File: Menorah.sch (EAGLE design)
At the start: 34 parts

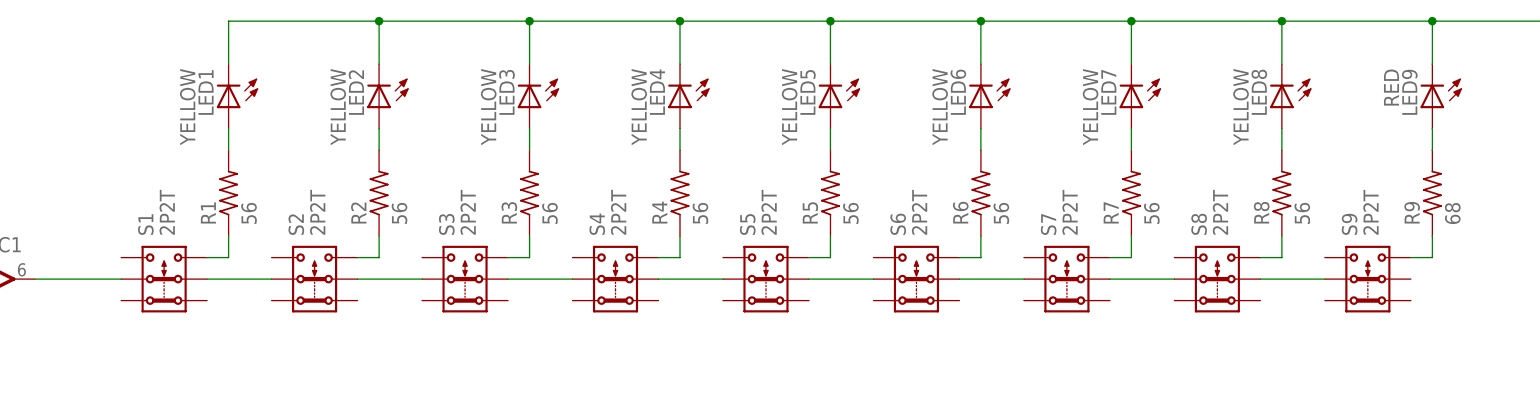
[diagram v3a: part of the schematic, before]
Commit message: replaced dpdt switch
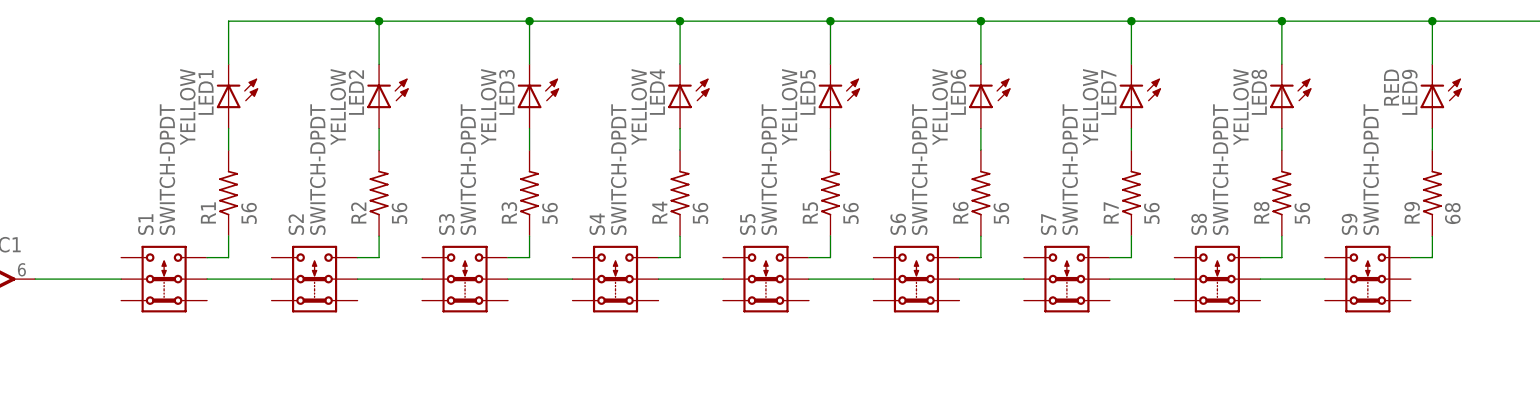
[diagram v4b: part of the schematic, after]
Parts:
- S1, S2, S3, S4, S5, S6, S7, S8, S9: value 2P2T -> SWITCH-DPDT; device switch:2P2T -> Menorah:SWITCH-DPDT
- S10: DIGIKEY (none) -> EG4791-ND
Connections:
- net N$10: now also S1.3; no longer S1.3.2
- net N$11: now also S2.3; no longer S2.3.2
- net N$12: now also S3.3; no longer S3.3.2
- net N$13: now also S4.3; no longer S4.3.2
- net N$14: now also S5.3; no longer S5.3.2
- net N$15: now also S6.3; no longer S6.3.2
- net N$16: now also S7.3; no longer S7.3.2
- net N$17: now also S8.3; no longer S8.3.2
- net N$18: now also S9.3; no longer S9.3.2
- net N$21: now also S1.5; no longer S1.2.1
- net N$23: now also S1.2, S2.5; no longer S1.2.2, S2.2.1
- net N$24: now also S2.2, S3.5; no longer S2.2.2, S3.2.1
- net N$25: now also S3.2, S4.5; no longer S3.2.2, S4.2.1
- net N$26: now also S4.2, S5.5; no longer S4.2.2, S5.2.1
- net N$27: now also S5.2, S6.5; no longer S5.2.2, S6.2.1
- net N$28: now also S6.2, S7.5; no longer S6.2.2, S7.2.1
- net N$29: now also S7.2, S8.5; no longer S7.2.2, S8.2.1
- net N$30: now also S8.2, S9.5; no longer S8.2.2, S9.2.1
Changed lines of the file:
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@@
 </classes>
 <parts>
-<part name="S1" library="switch" deviceset="2P2T" device="">
+<part name="S1" library="Menorah" deviceset="SWITCH-DPDT" device="">
 <attribute name="DIGIKEY" value="401-2002-1-ND"/>
 </part>
@@
 <attribute name="DIGIKEY" value="1276-5502-1-ND"/>
 </part>
-<part name="S2" library="switch" deviceset="2P2T" device="">
-<attribute name="DIGIKEY" value="401-2002-1-ND"/>
-</part>
-<part name="S3" library="switch" deviceset="2P2T" device="">
-<attribute name="DIGIKEY" value="401-2002-1-ND"/>
-</part>
-<part name="S4" library="switch" deviceset="2P2T" device="">
-<attribute name="DIGIKEY" value="401-2002-1-ND"/>
-</part>
-<part name="S5" library="switch" deviceset="2P2T" device="">
-<attribute name="DIGIKEY" value="401-2002-1-ND"/>
-</part>
-<part name="S6" library="switch" deviceset="2P2T" device="">
-<attribute name="DIGIKEY" value="401-2002-1-ND"/>
-</part>
-<part name="S7" library="switch" deviceset="2P2T" device="">
-<attribute name="DIGIKEY" value="401-2002-1-ND"/>
-</part>
-<part name="S8" library="switch" deviceset="2P2T" device="">
-<attribute name="DIGIKEY" value="401-2002-1-ND"/>
-</part>
-<part name="S9" library="switch" deviceset="2P2T" device="">
-<attribute name="DIGIKEY" value="401-2002-1-ND"/>
-</part>
-<part name="S10" library="Menorah" deviceset="SWITCH-SPST" device=""/>
+<part name="S2" library="Menorah" deviceset="SWITCH-DPDT" device="">
+<attribute name="DIGIKEY" value="401-2002-1-ND"/>
+</part>
+<part name="S3" library="Menorah" deviceset="SWITCH-DPDT" device="">
+<attribute name="DIGIKEY" value="401-2002-1-ND"/>
+</part>
+<part name="S4" library="Menorah" deviceset="SWITCH-DPDT" device="">
+<attribute name="DIGIKEY" value="401-2002-1-ND"/>
+</part>
+<part name="S5" library="Menorah" deviceset="SWITCH-DPDT" device="">
+<attribute name="DIGIKEY" value="401-2002-1-ND"/>
+</part>
+<part name="S6" library="Menorah" deviceset="SWITCH-DPDT" device="">
+<attribute name="DIGIKEY" value="401-2002-1-ND"/>
+</part>
+<part name="S7" library="Menorah" deviceset="SWITCH-DPDT" device="">
+<attribute name="DIGIKEY" value="401-2002-1-ND"/>
+</part>
+<part name="S8" library="Menorah" deviceset="SWITCH-DPDT" device="">
+<attribute name="DIGIKEY" value="401-2002-1-ND"/>
+</part>
+<part name="S9" library="Menorah" deviceset="SWITCH-DPDT" device="">
+<attribute name="DIGIKEY" value="401-2002-1-ND"/>
+</part>
+<part name="S10" library="Menorah" deviceset="SWITCH-SPST" device="">
+<attribute name="DIGIKEY" value="EG4791-ND"/>
+</part>
 </parts>
 <sheets>
@@
 </plain>
 <instances>
-<instance part="S1" gate="G$1" x="162.56" y="132.08" rot="R90">
+<instance part="S1" gate="S$1" x="162.56" y="132.08" rot="R90">
 <attribute name="DIGIKEY" x="162.56" y="132.08" size="1.778" layer="96" rot="R90" display="off"/>
 </instance>
@@
 <attribute name="DIGIKEY" x="294.64" y="142.24" size="1.778" layer="96" rot="R90" display="off"/>
 </instance>
-<instance part="S2" gate="G$1" x="180.34" y="132.08" rot="R90">
+<instance part="S2" gate="S$1" x="180.34" y="132.08" rot="R90">
 <attribute name="DIGIKEY" x="180.34" y="132.08" size="1.778" layer="96" rot="R90" display="off"/>
 </instance>
-<instance part="S3" gate="G$1" x="198.12" y="132.08" rot="R90">
+<instance part="S3" gate="S$1" x="198.12" y="132.08" rot="R90">
 <attribute name="DIGIKEY" x="198.12" y="132.08" size="1.778" layer="96" rot="R90" display="off"/>
 </instance>
-<instance part="S4" gate="G$1" x="215.9" y="132.08" rot="R90">
+<instance part="S4" gate="S$1" x="215.9" y="132.08" rot="R90">
 <attribute name="DIGIKEY" x="215.9" y="132.08" size="1.778" layer="96" rot="R90" display="off"/>
 </instance>
-<instance part="S5" gate="G$1" x="233.68" y="132.08" rot="R90">
+<instance part="S5" gate="S$1" x="233.68" y="132.08" rot="R90">
 <attribute name="DIGIKEY" x="233.68" y="132.08" size="1.778" layer="96" rot="R90" display="off"/>
 </instance>
-<instance part="S6" gate="G$1" x="251.46" y="132.08" rot="R90">
+<instance part="S6" gate="S$1" x="251.46" y="132.08" rot="R90">
 <attribute name="DIGIKEY" x="251.46" y="132.08" size="1.778" layer="96" rot="R90" display="off"/>
 </instance>
-<instance part="S7" gate="G$1" x="269.24" y="132.08" rot="R90">
+<instance part="S7" gate="S$1" x="269.24" y="132.08" rot="R90">
 <attribute name="DIGIKEY" x="269.24" y="132.08" size="1.778" layer="96" rot="R90" display="off"/>
 </instance>
-<instance part="S8" gate="G$1" x="287.02" y="132.08" rot="R90">
+<instance part="S8" gate="S$1" x="287.02" y="132.08" rot="R90">
 <attribute name="DIGIKEY" x="287.02" y="132.08" size="1.778" layer="96" rot="R90" display="off"/>
 </instance>
-<instance part="S9" gate="G$1" x="304.8" y="132.08" rot="R90">
+<instance part="S9" gate="S$1" x="304.8" y="132.08" rot="R90">
 <attribute name="DIGIKEY" x="304.8" y="132.08" size="1.778" layer="96" rot="R90" display="off"/>
 </instance>
-<instance part="S10" gate="G$1" x="63.5" y="134.62"/>
+<instance part="S10" gate="G$1" x="63.5" y="134.62">
+<attribute name="DIGIKEY" x="63.5" y="134.62" size="1.778" layer="96" display="off"/>
+</instance>
 </instances>
 <busses>
@@
 <segment>
 <pinref part="IC1" gate="A" pin="OUT"/>
-<pinref part="S1" gate="G$1" pin="2.1"/>
+<pinref part="S1" gate="S$1" pin="5"/>
 <wire x1="147.32" y1="132.08" x2="157.48" y2="132.08" width="0.1524" layer="91"/>
 </segment>
@@
 <net name="N$23" class="0">
 <segment>
-<pinref part="S1" gate="G$1" pin="2.2"/>
+<pinref part="S1" gate="S$1" pin="2"/>
 <wire x1="167.64" y1="132.08" x2="175.26" y2="132.08" width="0.1524" layer="91"/>
-<pinref part="S2" gate="G$1" pin="2.1"/>
+<pinref part="S2" gate="S$1" pin="5"/>
 </segment>
 </net>
@@
 <segment>
 <wire x1="185.42" y1="132.08" x2="193.04" y2="132.08" width="0.1524" layer="91"/>
-<pinref part="S2" gate="G$1" pin="2.2"/>
-<pinref part="S3" gate="G$1" pin="2.1"/>
+<pinref part="S2" gate="S$1" pin="2"/>
+<pinref part="S3" gate="S$1" pin="5"/>
 </segment>
 </net>
@@
 <segment>
 <wire x1="203.2" y1="132.08" x2="210.82" y2="132.08" width="0.1524" layer="91"/>
-<pinref part="S3" gate="G$1" pin="2.2"/>
-<pinref part="S4" gate="G$1" pin="2.1"/>
+<pinref part="S3" gate="S$1" pin="2"/>
+<pinref part="S4" gate="S$1" pin="5"/>
 </segment>
 </net>
@@
 <segment>
 <wire x1="220.98" y1="132.08" x2="228.6" y2="132.08" width="0.1524" layer="91"/>
-<pinref part="S4" gate="G$1" pin="2.2"/>
-<pinref part="S5" gate="G$1" pin="2.1"/>
+<pinref part="S4" gate="S$1" pin="2"/>
+<pinref part="S5" gate="S$1" pin="5"/>
 </segment>
 </net>
@@
 <segment>
 <wire x1="238.76" y1="132.08" x2="246.38" y2="132.08" width="0.1524" layer="91"/>
-<pinref part="S5" gate="G$1" pin="2.2"/>
-<pinref part="S6" gate="G$1" pin="2.1"/>
+<pinref part="S5" gate="S$1" pin="2"/>
+<pinref part="S6" gate="S$1" pin="5"/>
 </segment>
 </net>
@@
 <segment>
 <wire x1="256.54" y1="132.08" x2="264.16" y2="132.08" width="0.1524" layer="91"/>
-<pinref part="S6" gate="G$1" pin="2.2"/>
-<pinref part="S7" gate="G$1" pin="2.1"/>
+<pinref part="S6" gate="S$1" pin="2"/>
+<pinref part="S7" gate="S$1" pin="5"/>
 </segment>
 </net>
@@
 <segment>
 <wire x1="274.32" y1="132.08" x2="281.94" y2="132.08" width="0.1524" layer="91"/>
-<pinref part="S7" gate="G$1" pin="2.2"/>
-<pinref part="S8" gate="G$1" pin="2.1"/>
+<pinref part="S7" gate="S$1" pin="2"/>
+<pinref part="S8" gate="S$1" pin="5"/>
 </segment>
 </net>
@@
 <segment>
 <wire x1="292.1" y1="132.08" x2="299.72" y2="132.08" width="0.1524" layer="91"/>
-<pinref part="S8" gate="G$1" pin="2.2"/>
-<pinref part="S9" gate="G$1" pin="2.1"/>
+<pinref part="S8" gate="S$1" pin="2"/>
+<pinref part="S9" gate="S$1" pin="5"/>
 </segment>
 </net>
 <net name="N$10" class="0">
 <segment>
-<pinref part="S1" gate="G$1" pin="3.2"/>
+<pinref part="S1" gate="S$1" pin="3"/>
 <wire x1="167.64" y1="134.62" x2="170.18" y2="134.62" width="0.1524" layer="91"/>
 <pinref part="R1" gate="G$1" pin="1"/>
@@
 <wire x1="187.96" y1="134.62" x2="187.96" y2="137.16" width="0.1524" layer="91"/>
 <pinref part="R2" gate="G$1" pin="1"/>
-<pinref part="S2" gate="G$1" pin="3.2"/>
+<pinref part="S2" gate="S$1" pin="3"/>
 </segment>
 </net>
@@
 <wire x1="205.74" y1="134.62" x2="205.74" y2="137.16" width="0.1524" layer="91"/>
 <pinref part="R3" gate="G$1" pin="1"/>
-<pinref part="S3" gate="G$1" pin="3.2"/>
+<pinref part="S3" gate="S$1" pin="3"/>
 </segment>
 </net>
@@
 <wire x1="223.52" y1="134.62" x2="223.52" y2="137.16" width="0.1524" layer="91"/>
 <pinref part="R4" gate="G$1" pin="1"/>
-<pinref part="S4" gate="G$1" pin="3.2"/>
+<pinref part="S4" gate="S$1" pin="3"/>
 </segment>
 </net>
@@
 <wire x1="241.3" y1="134.62" x2="241.3" y2="137.16" width="0.1524" layer="91"/>
 <pinref part="R5" gate="G$1" pin="1"/>
-<pinref part="S5" gate="G$1" pin="3.2"/>
+<pinref part="S5" gate="S$1" pin="3"/>
 </segment>
 </net>
@@
 <wire x1="259.08" y1="134.62" x2="259.08" y2="137.16" width="0.1524" layer="91"/>
 <pinref part="R6" gate="G$1" pin="1"/>
-<pinref part="S6" gate="G$1" pin="3.2"/>
+<pinref part="S6" gate="S$1" pin="3"/>
 </segment>
 </net>
@@
 <wire x1="276.86" y1="134.62" x2="276.86" y2="137.16" width="0.1524" layer="91"/>
 <pinref part="R7" gate="G$1" pin="1"/>
-<pinref part="S7" gate="G$1" pin="3.2"/>
+<pinref part="S7" gate="S$1" pin="3"/>
 </segment>
 </net>
@@
 <wire x1="294.64" y1="134.62" x2="294.64" y2="137.16" width="0.1524" layer="91"/>
 <pinref part="R8" gate="G$1" pin="1"/>
-<pinref part="S8" gate="G$1" pin="3.2"/>
+<pinref part="S8" gate="S$1" pin="3"/>
 </segment>
 </net>
@@
 <pinref part="R9" gate="G$1" pin="1"/>
 <wire x1="312.42" y1="134.62" x2="312.42" y2="137.16" width="0.1524" layer="91"/>
-<pinref part="S9" gate="G$1" pin="3.2"/>
-</segment>
-</net>
+<pinref part="S9" gate="S$1" pin="3"/>
+</segment>
+</net>

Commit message: changed circircuit, updated pcb
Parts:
- removed G1: CR2032, Menorah:CR2032
- removed IC1: (no value), linear:1AMP_P7+4D
- removed R12: 100k, rcl:R-US_R0805
- added Q1: BUZ382, transistor-fet:BUZ382
- R1, R2, R3, R4, R5, R6, R7, R8: value 56 -> 100; DIGIKEY 1276-5502-1-ND -> 1276-5508-1-ND
- R11: value 51k -> 100; DIGIKEY 1276-5569-1-ND -> 1276-5508-1-ND
- R9: value 68 -> 100; DIGIKEY 1276-5504-1-ND -> 1276-5508-1-ND
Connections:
- removed net N$23: S1.2, S2.5
- removed net N$24: S2.2, S3.5
- removed net N$25: S3.2, S4.5
- removed net N$26: S4.2, S5.5
- removed net N$27: S5.2, S6.5
- removed net N$28: S6.2, S7.5
- removed net N$29: S7.2, S8.5
- removed net N$30: S8.2, S9.5
- net N$1: now also LED1.C, R1.1; no longer LED1.A, R1.2
- net N$10: now also R1.2; no longer R1.1
- net N$11: now also R2.2; no longer R2.1
- net N$12: now also R3.2; no longer R3.1
- net N$13: now also R4.2; no longer R4.1
- net N$14: now also R5.2; no longer R5.1
- net N$15: now also R6.2; no longer R6.1
- net N$16: now also R7.2; no longer R7.1
- net N$17: now also R8.2; no longer R8.1
- net N$18: now also R9.2; no longer R9.1
- net N$19: now also R11.2, S10.1@A, S10.1@B; no longer IC1.-IN, R11.1, R12.2
- net N$2: now also LED2.C, R2.1; no longer LED2.A, R2.2
- net N$21: now also Q1.D, S1.2, S2.2, S2.5, S3.2, S3.5, S4.2, S4.5, S5.2, S5.5, S6.2, S6.5, S7.2, S7.5, S8.2, S8.5, S9.2, S9.5; no longer IC1.OUT
- net N$22: now also Q1.G, R11.1; no longer IC1.+IN, S10.1@A, S10.1@B
- net N$3: now also LED3.C, R3.1; no longer LED3.A, R3.2
- net N$4: now also LED4.C, R4.1; no longer LED4.A, R4.2
- net N$5: now also LED5.C, R5.1; no longer LED5.A, R5.2
- net N$6: now also LED6.C, R6.1; no longer LED6.A, R6.2
- net N$7: now also LED7.C, R7.1; no longer LED7.A, R7.2
- net N$8: now also LED8.C, R8.1; no longer LED8.A, R8.2
- net N$9: now also LED9.C, R9.1; no longer LED9.A, R9.2
- net PE: now also LED1.A, LED2.A, LED3.A, LED4.A, LED5.A, LED6.A, LED7.A, LED8.A, LED9.A, Q1.S; no longer G1.-, IC1.V-, LED1.C, LED2.C, LED3.C, LED4.C, LED5.C, LED6.C, LED7.C, LED8.C, LED9.C, R11.2
- net VCC: no longer G1.+, IC1.V+, R12.1
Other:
- moved on the sheet: C1, LED1, LED2, LED3, LED4, LED5, LED6, LED7, LED8, LED9, R1, R10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

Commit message: design finished
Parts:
- Q1: value BUZ382 -> (none); device transistor-fet:BUZ382 -> transistors:2N7002A_SOT23
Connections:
- net PE: no longer LED1.A, LED2.A, LED3.A, LED4.A, LED5.A, LED6.A, LED7.A, LED8.A, LED9.A
- net VCC: now also LED1.A, LED2.A, LED3.A, LED4.A, LED5.A, LED6.A, LED7.A, LED8.A, LED9.A
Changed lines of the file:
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@@
 <attribute name="DIGIKEY" value="475-1415-1-ND"/>
 </part>
-<part name="GND" library="supply1" deviceset="PE" device=""/>
 <part name="C1" library="rcl" deviceset="C-US" device="C1206" value="100uF">
 <attribute name="DIGIKEY" value="490-4539-1-ND"/>
@@
 <attribute name="DIGIKEY" value="EG4791-ND"/>
 </part>
-<part name="Q1" library="transistor-fet" deviceset="BUZ382" device=""/>
 <part name="GND1" library="supply1" deviceset="PE" device=""/>
 <part name="R11" library="rcl" deviceset="R-US_" device="R0805" value="100">
@@
 <attribute name="DIGIKEY" value="1276-5508-1-ND"/>
 </part>
+<part name="P+2" library="supply1" deviceset="VCC" device=""/>
+<part name="Q1" library="transistors" deviceset="2N700*" device="_SOT23" technology="2A"/>
 </parts>
 <sheets>
@@
 <attribute name="DIGIKEY" x="312.42" y="154.94" size="1.778" layer="96" display="off"/>
 </instance>
-<instance part="GND" gate="M" x="327.66" y="152.4" smashed="yes"/>
 <instance part="C1" gate="G$1" x="83.82" y="119.38">
 <attribute name="DIGIKEY" x="83.82" y="119.38" size="1.778" layer="96" display="off"/>
@@
 <attribute name="DIGIKEY" x="63.5" y="127" size="1.778" layer="96" display="off"/>
 </instance>
-<instance part="Q1" gate="G$1" x="121.92" y="129.54"/>
-<instance part="GND1" gate="M" x="127" y="114.3" smashed="yes"/>
+<instance part="GND1" gate="M" x="116.84" y="114.3" smashed="yes"/>
 <instance part="R11" gate="G$1" x="76.2" y="127" rot="R180">
 <attribute name="DIGIKEY" x="76.2" y="127" size="1.778" layer="96" rot="R180" display="off"/>
@@
 <attribute name="DIGIKEY" x="312.42" y="142.24" size="1.778" layer="96" rot="R270" display="off"/>
 </instance>
+<instance part="P+2" gate="VCC" x="170.18" y="177.8"/>
+<instance part="Q1" gate="G$1" x="116.84" y="129.54"/>
 </instances>
 <busses>
@@
 <net name="PE" class="0">
 <segment>
+<pinref part="C1" gate="G$1" pin="2"/>
+<pinref part="GND2" gate="M" pin="PE"/>
+<wire x1="83.82" y1="114.3" x2="83.82" y2="109.22" width="0.1524" layer="91"/>
+</segment>
+<segment>
+<pinref part="GND5" gate="M" pin="PE"/>
+<pinref part="R10" gate="G$1" pin="1"/>
+<wire x1="96.52" y1="109.22" x2="96.52" y2="111.76" width="0.1524" layer="91"/>
+</segment>
+<segment>
+<pinref part="GND1" gate="M" pin="PE"/>
+<wire x1="116.84" y1="116.84" x2="116.84" y2="119.38" width="0.1524" layer="91"/>
+<pinref part="Q1" gate="G$1" pin="S"/>
+</segment>
+</net>
+<net name="VCC" class="0">
+<segment>
+<pinref part="P+1" gate="VCC" pin="VCC"/>
+<wire x1="48.26" y1="137.16" x2="48.26" y2="127" width="0.1524" layer="91"/>
+<pinref part="S10" gate="G$1" pin="0@A"/>
+<wire x1="55.88" y1="127" x2="48.26" y2="127" width="0.1524" layer="91"/>
+<pinref part="S10" gate="G$1" pin="0@B"/>
+<wire x1="55.88" y1="124.46" x2="55.88" y2="127" width="0.1524" layer="91"/>
+<junction x="55.88" y="127"/>
+</segment>
+<segment>
+<pinref part="P+2" gate="VCC" pin="VCC"/>
+<wire x1="170.18" y1="175.26" x2="170.18" y2="162.56" width="0.1524" layer="91"/>
 <wire x1="170.18" y1="162.56" x2="187.96" y2="162.56" width="0.1524" layer="91"/>
 <wire x1="187.96" y1="162.56" x2="205.74" y2="162.56" width="0.1524" layer="91"/>
@@
 <wire x1="276.86" y1="162.56" x2="294.64" y2="162.56" width="0.1524" layer="91"/>
 <wire x1="294.64" y1="162.56" x2="312.42" y2="162.56" width="0.1524" layer="91"/>
-<wire x1="312.42" y1="162.56" x2="327.66" y2="162.56" width="0.1524" layer="91"/>
-<wire x1="327.66" y1="162.56" x2="327.66" y2="154.94" width="0.1524" layer="91"/>
-<pinref part="GND" gate="M" pin="PE"/>
 <pinref part="LED1" gate="G$1" pin="A"/>
 <wire x1="170.18" y1="157.48" x2="170.18" y2="162.56" width="0.1524" layer="91"/>
@@
 <pinref part="LED9" gate="G$1" pin="A"/>
 <wire x1="312.42" y1="157.48" x2="312.42" y2="162.56" width="0.1524" layer="91"/>
-<junction x="312.42" y="162.56"/>
 <pinref part="LED8" gate="G$1" pin="A"/>
 <wire x1="294.64" y1="157.48" x2="294.64" y2="162.56" width="0.1524" layer="91"/>
 <junction x="294.64" y="162.56"/>
-</segment>
-<segment>
-<pinref part="C1" gate="G$1" pin="2"/>
-<pinref part="GND2" gate="M" pin="PE"/>
-<wire x1="83.82" y1="114.3" x2="83.82" y2="109.22" width="0.1524" layer="91"/>
-</segment>
-<segment>
-<pinref part="GND5" gate="M" pin="PE"/>
-<pinref part="R10" gate="G$1" pin="1"/>
-<wire x1="96.52" y1="109.22" x2="96.52" y2="111.76" width="0.1524" layer="91"/>
-</segment>
-<segment>
-<pinref part="GND1" gate="M" pin="PE"/>
-<pinref part="Q1" gate="G$1" pin="S"/>
-<wire x1="127" y1="116.84" x2="127" y2="127" width="0.1524" layer="91"/>
-</segment>
-</net>
-<net name="VCC" class="0">
-<segment>
-<pinref part="P+1" gate="VCC" pin="VCC"/>
-<wire x1="48.26" y1="137.16" x2="48.26" y2="127" width="0.1524" layer="91"/>
-<pinref part="S10" gate="G$1" pin="0@A"/>
-<wire x1="55.88" y1="127" x2="48.26" y2="127" width="0.1524" layer="91"/>
-<pinref part="S10" gate="G$1" pin="0@B"/>
-<wire x1="55.88" y1="124.46" x2="55.88" y2="127" width="0.1524" layer="91"/>
-<junction x="55.88" y="127"/>
+<junction x="170.18" y="162.56"/>
 </segment>
 </net>
@@
 <wire x1="312.42" y1="132.08" x2="309.88" y2="132.08" width="0.1524" layer="91"/>
 <pinref part="Q1" gate="G$1" pin="D"/>
-<wire x1="152.4" y1="132.08" x2="127" y2="132.08" width="0.1524" layer="91"/>
+<wire x1="116.84" y1="139.7" x2="152.4" y2="139.7" width="0.1524" layer="91"/>
+<wire x1="152.4" y1="139.7" x2="152.4" y2="132.08" width="0.1524" layer="91"/>
 </segment>
 </net>
@@
 <wire x1="96.52" y1="127" x2="83.82" y2="127" width="0.1524" layer="91"/>
 <wire x1="96.52" y1="121.92" x2="96.52" y2="127" width="0.1524" layer="91"/>
-<pinref part="Q1" gate="G$1" pin="G"/>
-<wire x1="116.84" y1="127" x2="96.52" y2="127" width="0.1524" layer="91"/>
+<wire x1="106.68" y1="127" x2="96.52" y2="127" width="0.1524" layer="91"/>
 <junction x="96.52" y="127"/>
 <pinref part="R11" gate="G$1" pin="1"/>
 <wire x1="81.28" y1="127" x2="83.82" y2="127" width="0.1524" layer="91"/>
 <junction x="83.82" y="127"/>
-</segment>
-</net>
+<pinref part="Q1" gate="G$1" pin="G"/>
+</segment>
+</net>
